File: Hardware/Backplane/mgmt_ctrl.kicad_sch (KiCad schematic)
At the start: 6 parts, among them J1901 Conn_01x03, U1901 SN74LVC1G08DBVR, U1902 CH32V003FxPx

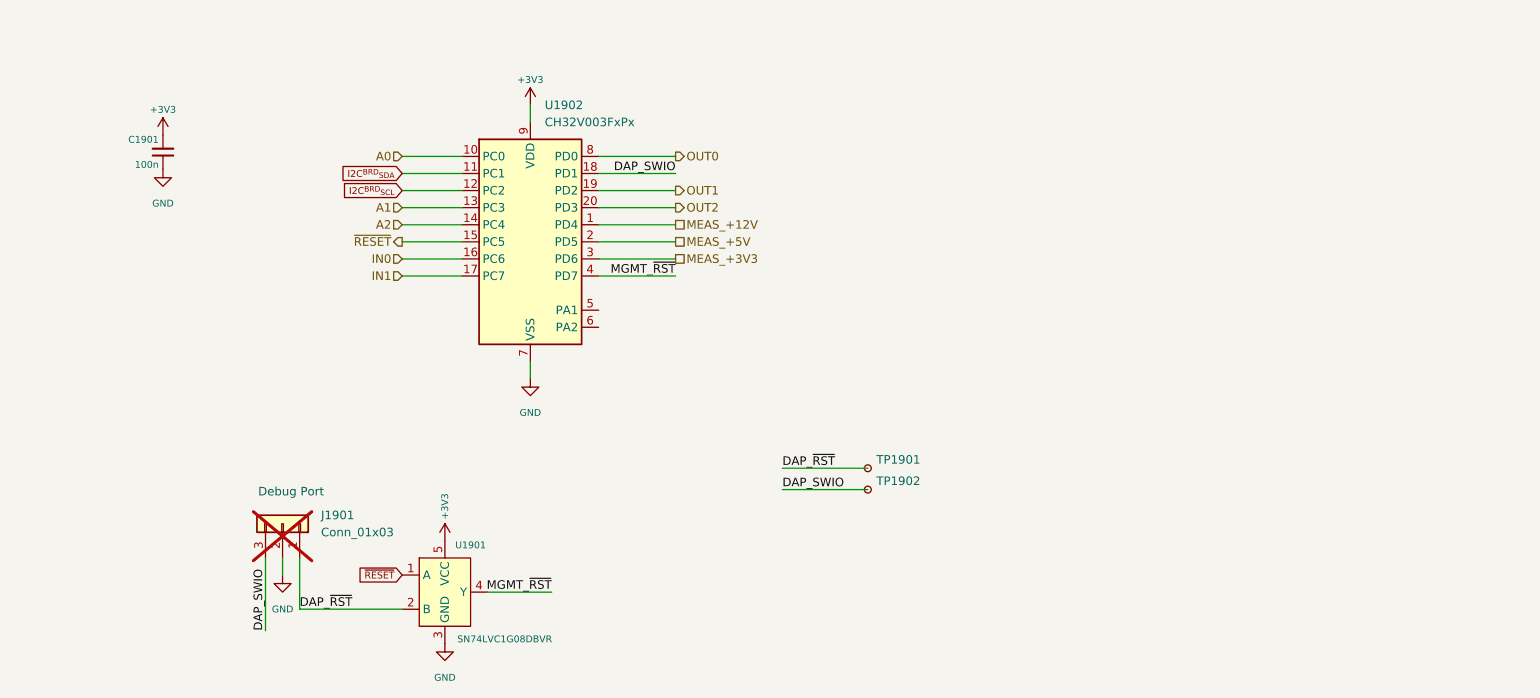
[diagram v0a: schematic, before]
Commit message: Cleans up schematic, adds clean RESET gating
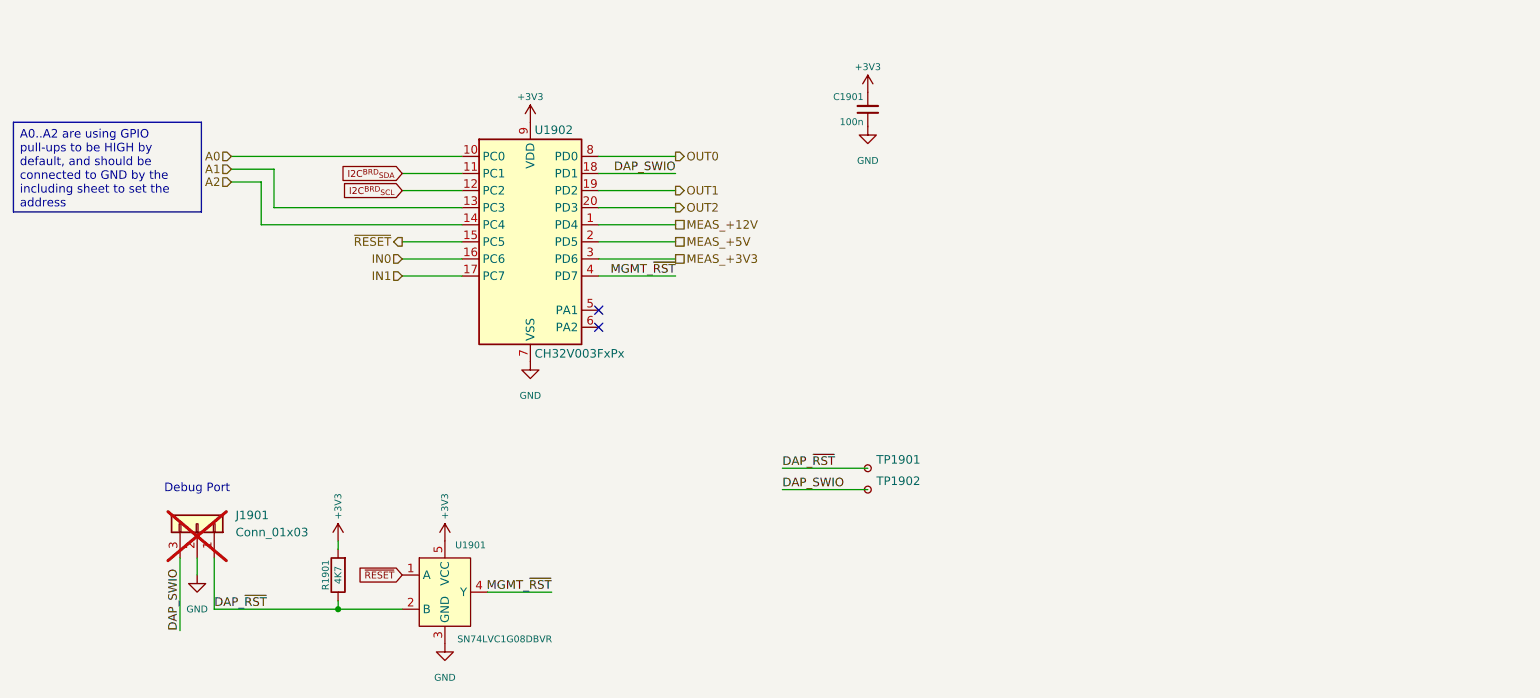
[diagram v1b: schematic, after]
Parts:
- added R1901: 4K7, Resistor_SMD:R_0603_1608Metric, symbol Device:R
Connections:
- net +3V3: now also R1901.2
- net DAP_~{RST}: now also R1901.1
- no-connect marks 0 -> 2
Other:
- company: (none) -> Ashet Technologies
- title: (none) -> I²C Power & Reset Management Controller
- moved on the sheet: C1901, J1901

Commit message: Updates backplane: Improves voltage measurement dividers, replaces DS1307+ RTC with a much cheaper one, replaces 8 MHz global clock with 48 MHz global clock
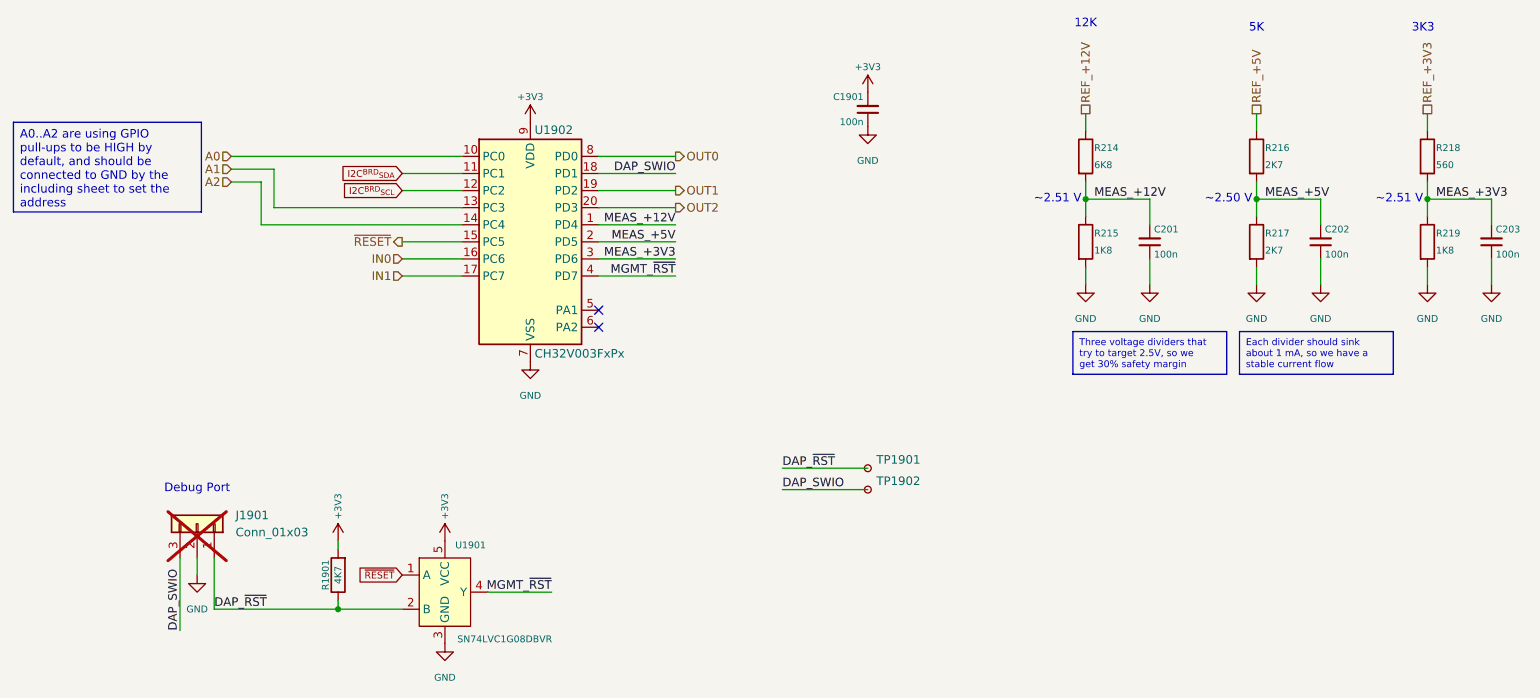
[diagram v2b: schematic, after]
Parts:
- added C201, C202, C203: 100n, Capacitor_SMD:C_0603_1608Metric, symbol Device:C_Small
- added R214: 6K8, Resistor_SMD:R_0603_1608Metric, symbol Device:R
- added R215, R219: 1K8, Resistor_SMD:R_0603_1608Metric, symbol Device:R
- added R216, R217: 2K7, Resistor_SMD:R_0603_1608Metric, symbol Device:R
- added R218: 560, Resistor_SMD:R_0603_1608Metric, symbol Device:R
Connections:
- net GND: now also C201.1, C202.1, C203.1, R215.2, R217.2, R219.2
- net MEAS_+12V: now also C201.2, R214.2, R215.1
- net MEAS_+3V3: now also C203.2, R218.2, R219.1
- net MEAS_+5V: now also C202.2, R216.2, R217.1
- new net REF_+12V: R214.1
- new net REF_+3V3: R218.1
- new net REF_+5V: R216.1
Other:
- note added: "12K"
- note added: "3K3"
- note added: "5K"
- note added: "~2.50 V"
- note added: "~2.51 V"

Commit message: Refactors clock system to use AND gates for clock tree spanning and gating.
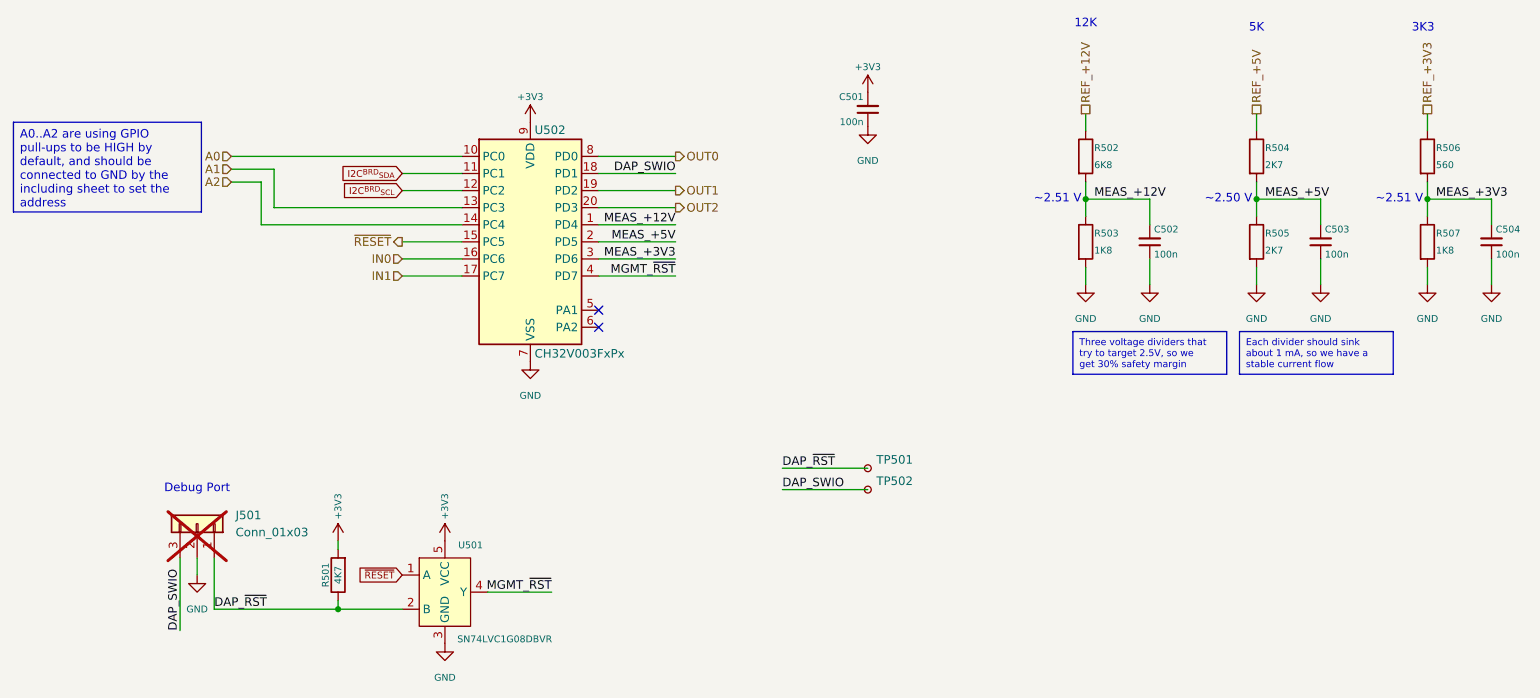
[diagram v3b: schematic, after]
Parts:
- renumbered C1901 to C501, C201 to C502, C202 to C503, C203 to C504, J1901 to J501, R1901 to R501, R214 to R502, R215 to R503, R216 to R504, R217 to R505, R218 to R506, R219 to R507, TP1901 to TP501, TP1902 to TP502, U1901 to U501, U1902 to U502

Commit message: Some cleanups of Backplane schematic: Adds DigiKey part numbers, removes unnecessary properties, marks test points as excluded from BOM
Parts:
- TP501, TP502: now left out of the parts list
- U501: Digikey Part No (none) -> 296-11601-1-ND
- U502: Digikey Part No (none) -> 1188-SMDICCH32V003F4P6-ND
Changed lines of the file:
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@@
 			)
 		)
-		(property "Datasheet" "~"
+		(property "Datasheet" ""
 			(at 187.325 50.8 0)
 			(effects
@@
 			)
 		)
-		(property "Datasheet" "~"
+		(property "Datasheet" ""
 			(at 212.725 50.8 0)
 			(effects
@@
 			)
 		)
-		(property "Datasheet" "~"
+		(property "Datasheet" ""
 			(at 238.125 50.8 0)
 			(effects
@@
 			)
 		)
-		(property "Datasheet" "~"
+		(property "Datasheet" ""
 			(at 203.2 50.8 0)
 			(effects
@@
 			)
 		)
-		(property "Datasheet" "~"
+		(property "Datasheet" ""
 			(at 177.8 50.8 0)
 			(effects
@@
 			)
 		)
-		(property "Datasheet" "~"
+		(property "Datasheet" ""
 			(at 228.6 50.8 0)
 			(effects
@@
 			)
 		)
-		(property "Datasheet" "~"
+		(property "Datasheet" ""
 			(at 203.2 38.1 0)
 			(effects
@@
 			)
 		)
-		(property "Datasheet" "~"
+		(property "Datasheet" ""
 			(at 145.415 31.115 0)
 			(effects
@@
 			)
 		)
-		(property "Datasheet" "~"
+		(property "Datasheet" ""
 			(at 66.675 100.33 0)
 			(effects
@@
 			)
 		)
-		(property "Datasheet" "~"
+		(property "Datasheet" ""
 			(at 228.6 38.1 0)
 			(effects
@@
 		(unit 1)
 		(exclude_from_sim no)
-		(in_bom yes)
+		(in_bom no)
 		(on_board yes)
 		(dnp no)
@@
 		)
 		(property "Description" "CH32V003 series are industrial-grade general-purpose microcontrollers designed based on 32-bit RISC-V instruction set and architecture. It adopts QingKe V2A core, RV32EC instruction set, and supports 2 levels of interrupt nesting. The series are mounted with rich peripheral interfaces and function modules. Its internal organizational structure meets the low-cost and low-power embedded application scenarios."
+			(at 95.25 50.8 0)
+			(effects
+				(font
+					(size 1.27 1.27)
+				)
+				(hide yes)
+			)
+		)
+		(property "Digikey Part No" "1188-SMDICCH32V003F4P6-ND"
 			(at 95.25 50.8 0)
 			(effects
@@
 			)
 		)
-		(property "Datasheet" "~"
+		(property "Datasheet" ""
 			(at 177.8 38.1 0)
 			(effects
@@
 		(unit 1)
 		(exclude_from_sim no)
-		(in_bom yes)
+		(in_bom no)
 		(on_board yes)
 		(dnp no)
@@
 			(effects
 				(font
+					(size 1.27 1.27)
+				)
+				(hide yes)
+			)
+		)
+		(property "Digikey Part No" "296-11601-1-ND"
+			(at 82.55 102.87 0)
+			(effects
+				(font
